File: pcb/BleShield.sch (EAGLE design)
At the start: 29 parts, among them Q1 32.768K, 10ppm, SW1 SPST_TACT-EVQQ2, SW2 SPST_TACT-EVQQ2, U1 ARDUINO_SHIELDNOHOLES

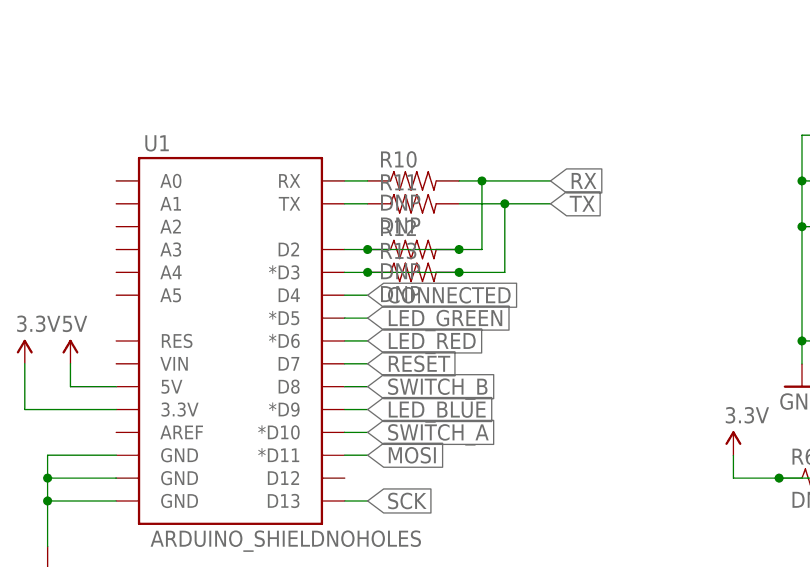
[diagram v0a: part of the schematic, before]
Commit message: Put the 47k resistors in for the pick&place machine
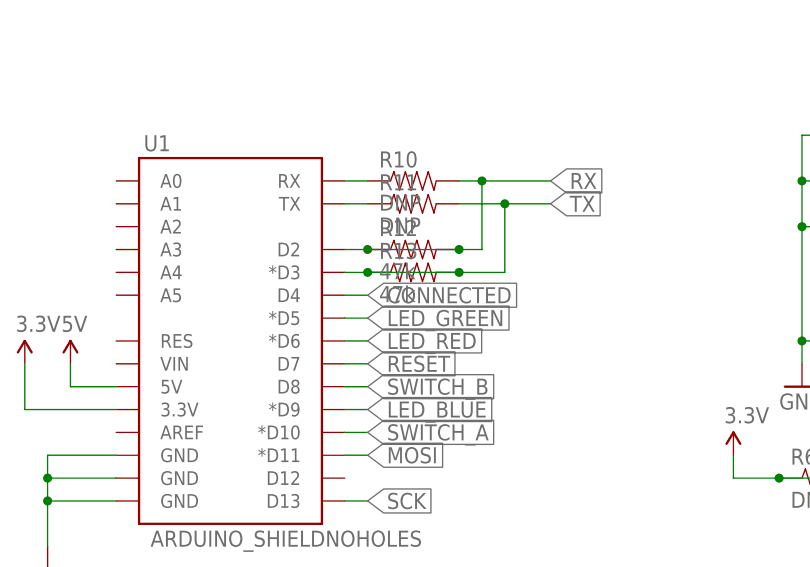
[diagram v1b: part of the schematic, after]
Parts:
- R12, R13: value DNP -> 47k
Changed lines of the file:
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@@
 <part name="R10" library="SparkFun" deviceset="RESISTOR" device="0805-RES" value="DNP"/>
 <part name="R11" library="SparkFun" deviceset="RESISTOR" device="0805-RES" value="DNP"/>
-<part name="R12" library="SparkFun" deviceset="RESISTOR" device="0805-RES" value="DNP"/>
-<part name="R13" library="SparkFun" deviceset="RESISTOR" device="0805-RES" value="DNP"/>
+<part name="R12" library="SparkFun" deviceset="RESISTOR" device="0805-RES" value="47k"/>
+<part name="R13" library="SparkFun" deviceset="RESISTOR" device="0805-RES" value="47k"/>
 <part name="JP1" library="SparkFun" deviceset="M05" device="1.27MM"/>
 <part name="JP2" library="SparkFun" deviceset="M04" device="1.27MM"/>
